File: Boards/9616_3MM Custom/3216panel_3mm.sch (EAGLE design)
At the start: 452 parts, among them U1 74HC164D, U10 74HCT04D, U11 HT1632C, U12 HT1632C, U13 74HC164D, U14 HT1632C, U15 HT1632C, U16 74HCT04D, U17 HT1632C, U18 HT1632C, U2 HT1632C, U3 HT1632C, U4 74HCT04D, U5 HT1632C, U6 HT1632C, U7 74HC164D, U8 HT1632C, U9 HT1632C

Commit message: Finished routing board (for Sierra Circuits/PCBCart.com specs)
Signed-off-by: Evan Richardson <erichardson@savi.com>
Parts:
- C1, C2: value 10pf -> 10pF
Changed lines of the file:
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@@
 <?xml version="1.0" encoding="utf-8"?>
 <!DOCTYPE eagle SYSTEM "eagle.dtd">
-<eagle version="6.0">
+<eagle version="6.1">
 <drawing>
 <settings>
@@
 </variantdefs>
 <classes>
-<class number="0" name="default" width="0.2" drill="0.2">
-<clearance class="0" value="0.2"/>
+<class number="0" name="default" width="0.254" drill="0.254">
+<clearance class="0" value="0.3048"/>
 </class>
-<class number="1" name="+5V" width="0.3048" drill="0.2">
-<clearance class="1" value="0.2"/>
+<class number="1" name="+5V" width="0.3556" drill="0.254">
+<clearance class="1" value="0.3048"/>
+</class>
+<class number="2" name="GND" width="0.3048" drill="0.254">
+<clearance class="2" value="0.3048"/>
 </class>
 </classes>
@@
 <part name="GND7" library="supply1" deviceset="GND" device=""/>
 <part name="GND8" library="supply1" deviceset="GND" device=""/>
-<part name="C2" library="SparkFun" deviceset="CAP" device="0805" value="10pf"/>
+<part name="C2" library="SparkFun" deviceset="CAP" device="0805" value="10pF"/>
 <part name="GND9" library="supply1" deviceset="GND" device=""/>
-<part name="C1" library="SparkFun" deviceset="CAP" device="0805" value="10pf"/>
+<part name="C1" library="SparkFun" deviceset="CAP" device="0805" value="10pF"/>
 <part name="P+5" library="supply1" deviceset="+5V" device=""/>
 <part name="C4" library="SparkFun" deviceset="CAP" device="0805" value="100nF"/>
@@
 </segment>
 </net>
-<net name="GND" class="0">
+<net name="GND" class="2">
 <segment>
 <pinref part="U2" gate="G$1" pin="VSS"/>
@@
 </segment>
 </net>
-<net name="GND" class="0">
+<net name="GND" class="2">
 <segment>
 <pinref part="U9" gate="G$1" pin="VSS"/>
@@
 </busses>
 <nets>
-<net name="GND" class="0">
+<net name="GND" class="2">
 <segment>
 <pinref part="U15" gate="G$1" pin="VSS"/>

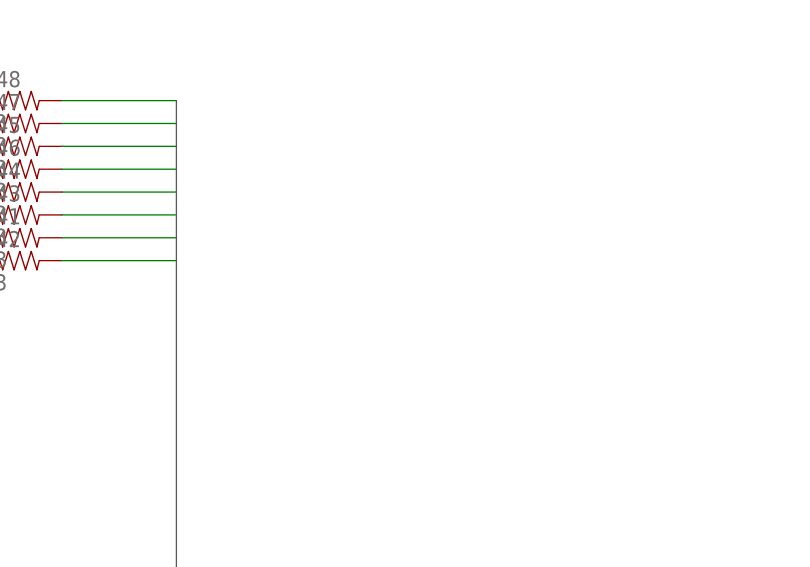
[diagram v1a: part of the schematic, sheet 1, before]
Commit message: added fiducial marks increased 5V supply to 16mil
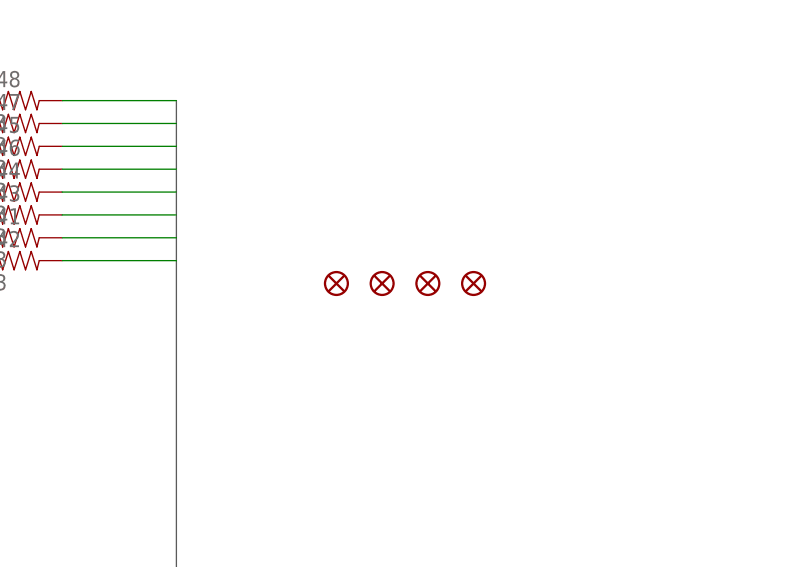
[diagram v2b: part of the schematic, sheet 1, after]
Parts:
- added JP1, JP2, JP3, JP4: FIDUCIAL1X2.5, SparkFun-Aesthetics:FIDUCIAL1X2.5
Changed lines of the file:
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@@
 <part name="FRAME2" library="frames" deviceset="FRAME_C_L" device=""/>
 <part name="FRAME3" library="frames" deviceset="FRAME_C_L" device=""/>
+<part name="JP1" library="SparkFun-Aesthetics" deviceset="FIDUCIAL" device="1X2.5"/>
+<part name="JP2" library="SparkFun-Aesthetics" deviceset="FIDUCIAL" device="1X2.5"/>
+<part name="JP3" library="SparkFun-Aesthetics" deviceset="FIDUCIAL" device="1X2.5"/>
+<part name="JP4" library="SparkFun-Aesthetics" deviceset="FIDUCIAL" device="1X2.5"/>
 </parts>
 <sheets>
@@
 <instance part="FRAME1" gate="G$1" x="-276.86" y="-220.98"/>
 <instance part="FRAME1" gate="G$2" x="175.26" y="-220.98"/>
+<instance part="JP1" gate="G$1" x="177.8" y="142.24"/>
+<instance part="JP2" gate="G$1" x="182.88" y="142.24"/>
+<instance part="JP3" gate="G$1" x="187.96" y="142.24"/>
+<instance part="JP4" gate="G$1" x="193.04" y="142.24"/>
 </instances>
 <busses>

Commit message: added missing connection between pins 19 on LED matrix and pin 23 on controller for top right 2 displays
Signed-off-by: evanrich <erichardson@savi.com>
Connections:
- net ANODE_B1: now also U2.COM1
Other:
- moved on the sheet: C11, C12
